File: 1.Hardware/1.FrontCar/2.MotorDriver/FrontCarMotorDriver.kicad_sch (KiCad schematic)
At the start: 10 parts

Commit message: drv
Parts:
- removed IC?: DRV8701ERGER, Package_DFN_QFN:QFN-24-1EP_4x4mm_P0.5mm_EP2.65x2.65mm_ThermalVias, symbol ErBW_s:DRV8701ERGER
- added C? (x3): 1uF, symbol Device:C_Small
- added C?: 10uF, symbol Device:C_Polarized_Small_US
- added C? (x5): (no value), symbol Device:C_Small
- added C? (x2): 0.1uF, symbol Device:C_Small
- added C?: (no value), symbol Device:C_Polarized_Small_US
- added D? (x2): 1N5819WS, Diode_SMD:D_SOD-323, symbol Diode:1N5819WS
- added IC?: DRV8701ERGER, Package_DFN_QFN:QFN-24-1EP_4x4mm_P0.5mm_EP2.65x2.65mm_ThermalVias, symbol ErBW_s:DRV8701ERGER
- added M? (x2): Motor_DC, symbol Motor:Motor_DC
- added Q? (x4): NMOS, ErBW_s:TPH1R403NL, symbol Device:Q_NMOS_GDS
- added Q? (x3): (no value), ErBW_s:TPH1R403NL, symbol Device:Q_NMOS_GDS
- added Q?: (no value), symbol Device:Q_NMOS_GDS
- added R?: (no value), symbol Device:R_Small
- added R?: 50mR, symbol Device:R_Small
- IC?: value (none) -> SN74LVC244APW; footprint (none) -> SOP65P640X120-20N
- IC?: value (none) -> DRV8701ERGER; footprint (none) -> Package_DFN_QFN:QFN-24-1EP_4x4mm_P0.5mm_EP2.65x2.65mm_ThermalVias
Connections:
- net GNDPWR: now also IC?.16 (GND_2), IC?.20 (SN), IC?.25 (GND_3), IC?.5 (GND_1), C?.1, C?.1, C?.2, C?.2, C?.2, C?.2, C?.2, C?.2, IC?.16 (GND_2), IC?.20 (SN), IC?.25 (GND_3), IC?.5 (GND_1), R?.2, R?.2
- net at IC?.1 (VM): now also C?.1, C?.1, C?.2, D?.1 (K)
- net at IC?.12 (IDRIVE): now also IC?.6 (VREF), IC?.7 (AVDD), C?.1
- net at IC?.17 (GH1): now also Q?.1 (G)
- net at IC?.18 (SH1): now also M?.2 (-), Q?.2 (D), Q?.3 (S)
- net at IC?.19 (GL1): now also Q?.1 (G)
- net at IC?.2 (VCP): now also C?.2
- net at IC?.21 (SP): now also Q?.2 (D), Q?.3 (S), R?.1
- net at IC?.22 (GL2): now also Q?.1 (G)
- net at IC?.23 (SH2): now also M?.1 (+), Q?.2 (D), Q?.3 (S)
- net at IC?.24 (GH2): now also Q?.1 (G)
- net at IC?.3 (CPH): now also C?.1
- net at IC?.4 (CPL): now also C?.2
- net at IC?.8 (DVDD): now also C?.1
- new net: C?.1, C?.1, C?.2, D?.1 (K), IC?.1 (VM)
- new net: C?.2, IC?.2 (VCP)
- new net: IC?.23 (SH2), M?.1 (+), Q?.2 (D), Q?.3 (S)
- new net: IC?.18 (SH1), M?.2 (-), Q?.2 (D), Q?.3 (S)
- new net: IC?.19 (GL1), Q?.1 (G)
- new net: IC?.21 (SP), Q?.2 (D), Q?.3 (S), R?.1
- new net: C?.1, IC?.8 (DVDD)
- new net: C?.1, IC?.12 (IDRIVE), IC?.6 (VREF), IC?.7 (AVDD)
- new net: IC?.17 (GH1), Q?.1 (G)
- new net: IC?.22 (GL2), Q?.1 (G)
- new net: IC?.24 (GH2), Q?.1 (G)
- new net: C?.1, IC?.3 (CPH)
- new net: C?.2, IC?.4 (CPL)
- no-connect marks 0 -> 6
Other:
- moved on the sheet: C?, D?, IC?, R?, U?

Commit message: 电池接口
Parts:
- added C?: (no value), symbol Device:C_Polarized_Small_US
- added J?: (no value), symbol Connector_Generic:Conn_01x02
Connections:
- net +5V is gone; now on net +7.5V: C?.1, C?.1, U?.3 (VI)
- net GNDPWR: now also C?.2, J?.2 (Pin_2)
- net +7.5V: now reaches Q?.3 (S)
- net +7.5V: now also D?.2 (A), D?.2 (A), Q?.2 (D), Q?.2 (D), Q?.3 (S), C?.1, J?.1 (Pin_1)
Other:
- moved on the sheet: C?, D?, IC?, R?, U?

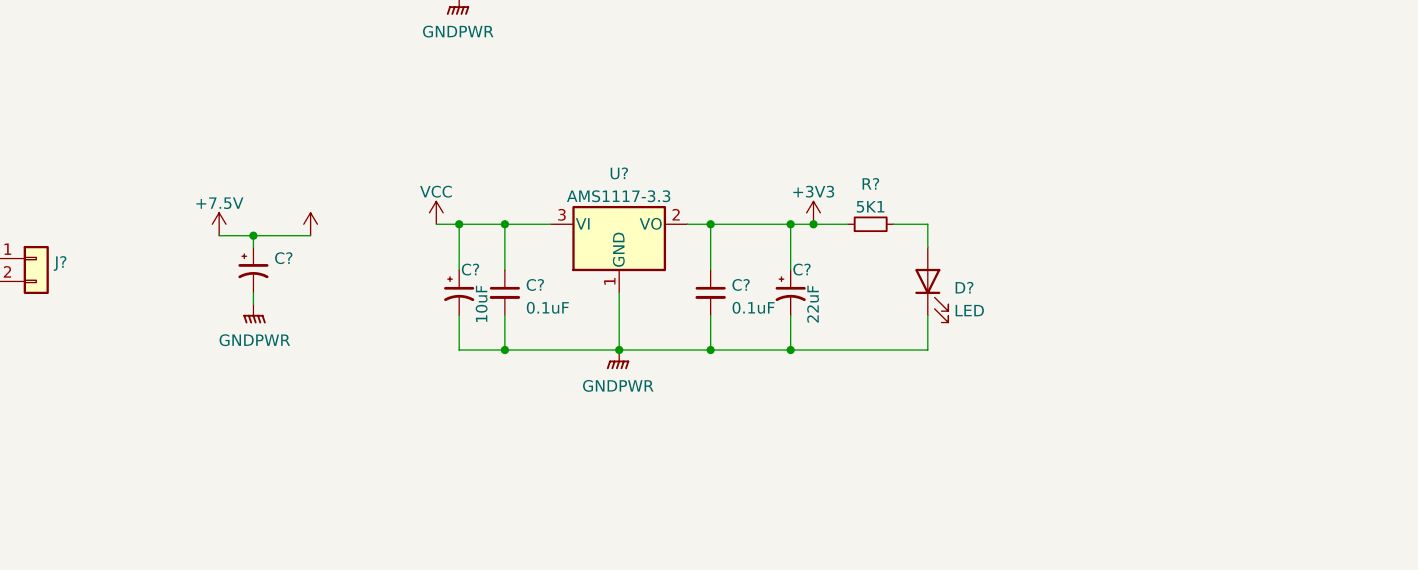
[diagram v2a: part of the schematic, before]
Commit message: 增加一个电源接口
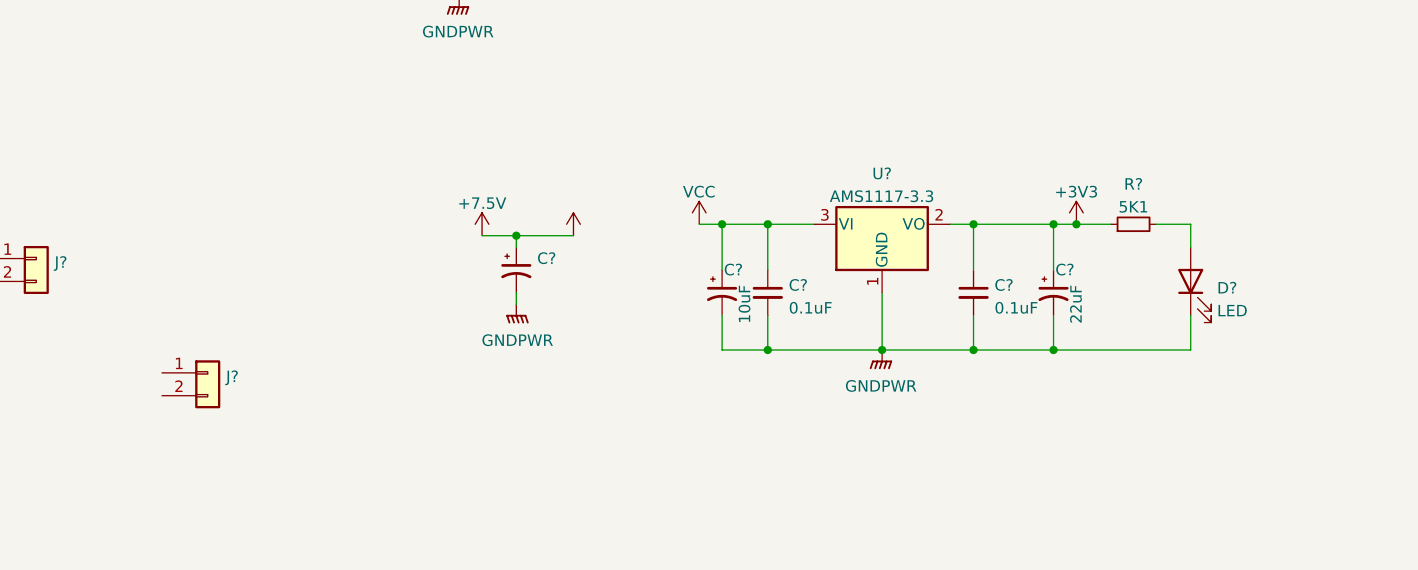
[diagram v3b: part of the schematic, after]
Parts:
- added J?: (no value), symbol Connector_Generic:Conn_01x02
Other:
- moved on the sheet: C?, D?, R?, U?

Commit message: 驱动板电源
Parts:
- added D?: (no value), symbol Diode:1N4148W
- added D?: LED, symbol Device:LED
- added R?: (no value), symbol Device:R_Small
- added SW?: SW_SPDT, symbol Switch:SW_SPDT
- added SW?: (no value), symbol Switch:SW_SPDT
- C?: value (none) -> 470uF
- C? (x3): value (none) -> 1uF
- C? (x2): value (none) -> 0.1uF
- C?: value (none) -> 10uF
- J?: value (none) -> Conn_01x02; footprint (none) -> Connector_AMASS:AMASS_XT30U-F_1x02_P5.0mm_Vertical
- J?: value (none) -> Conn_01x02; footprint (none) -> ErBW_s:BatteryHolder_2x18650
- Q? (x3): value (none) -> NMOS
- Q?: value (none) -> NMOS; footprint (none) -> ErBW_s:TPH1R403NL
- R?: value (none) -> 50mR
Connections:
- net +3V3: now also SW?.2 (B)
- net +7.5V: now also J?.1 (Pin_1), SW?.2 (B); no longer C?.1, C?.1, C?.1, D?.2 (A), D?.2 (A), Q?.2 (D), Q?.2 (D), Q?.3 (S), Q?.3 (S), U?.3 (VI)
- net GNDPWR: now also J?.2 (Pin_2), D?.1 (K)
- net WKUP: now reaches IC?.13 (NSLEEP)
- net WKUP: now also IC?.13 (NSLEEP), R?.1, SW?.1 (A)
- new net: C?.1, D?.2 (A), SW?.1 (A)
- new net: D?.2 (A), R?.2
- new net VCC: C?.1, C?.1, D?.1 (K), D?.2 (A), D?.2 (A), Q?.2 (D), Q?.2 (D), Q?.3 (S), Q?.3 (S), U?.3 (VI)
- no-connect marks 6 -> 8
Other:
- moved on the sheet: C?, D?, J?, R?, U?

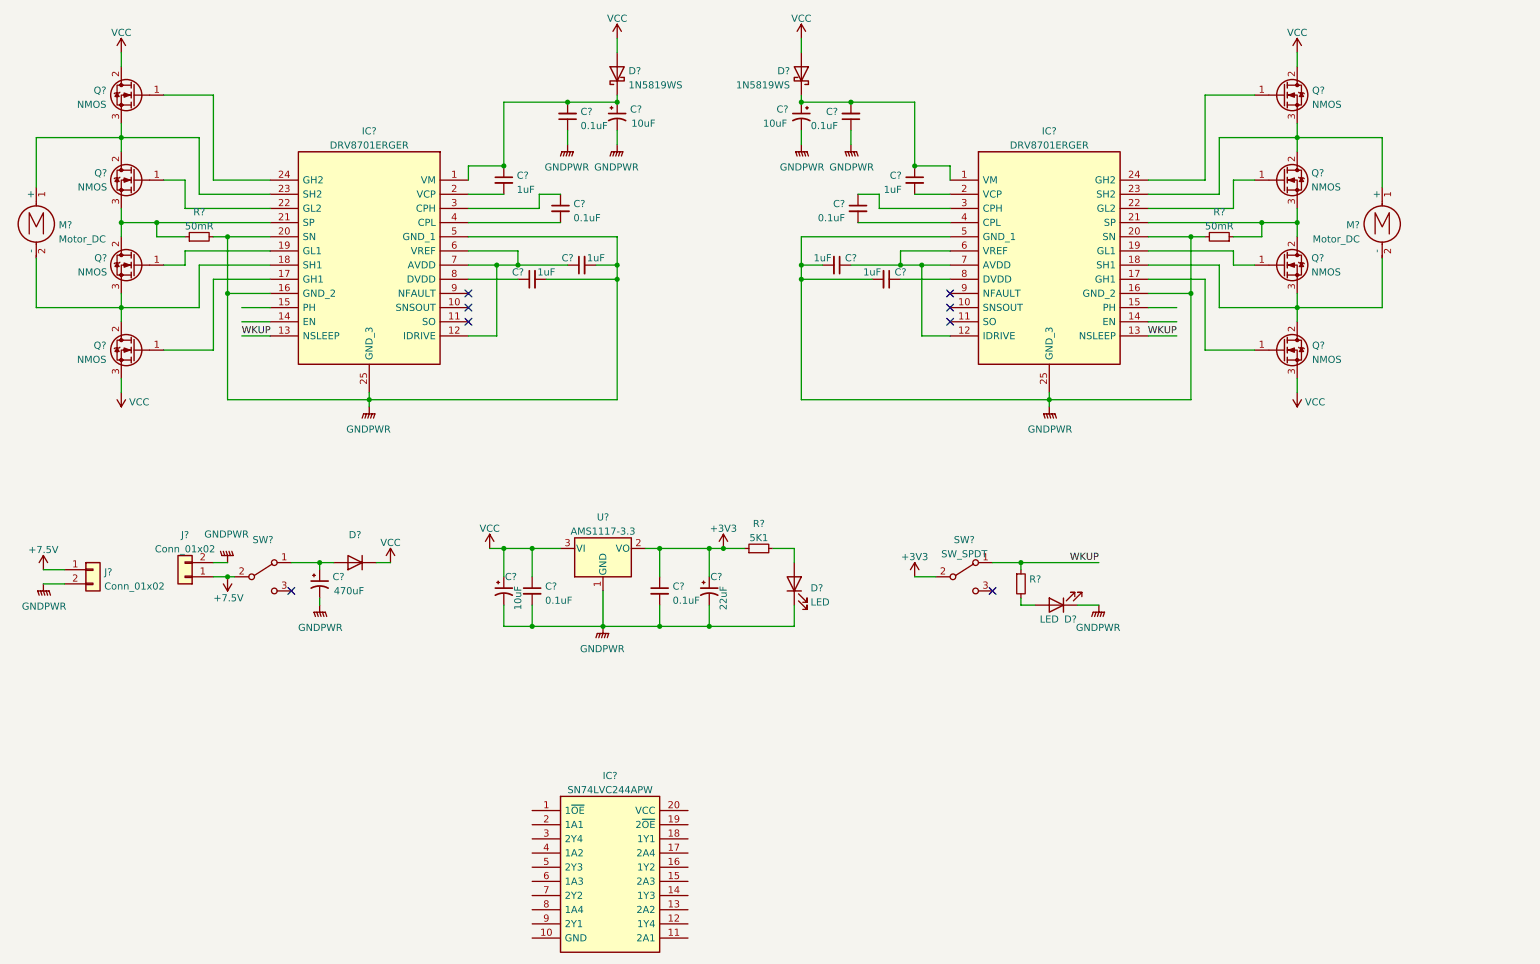
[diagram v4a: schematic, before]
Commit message: 驱动原理图完成
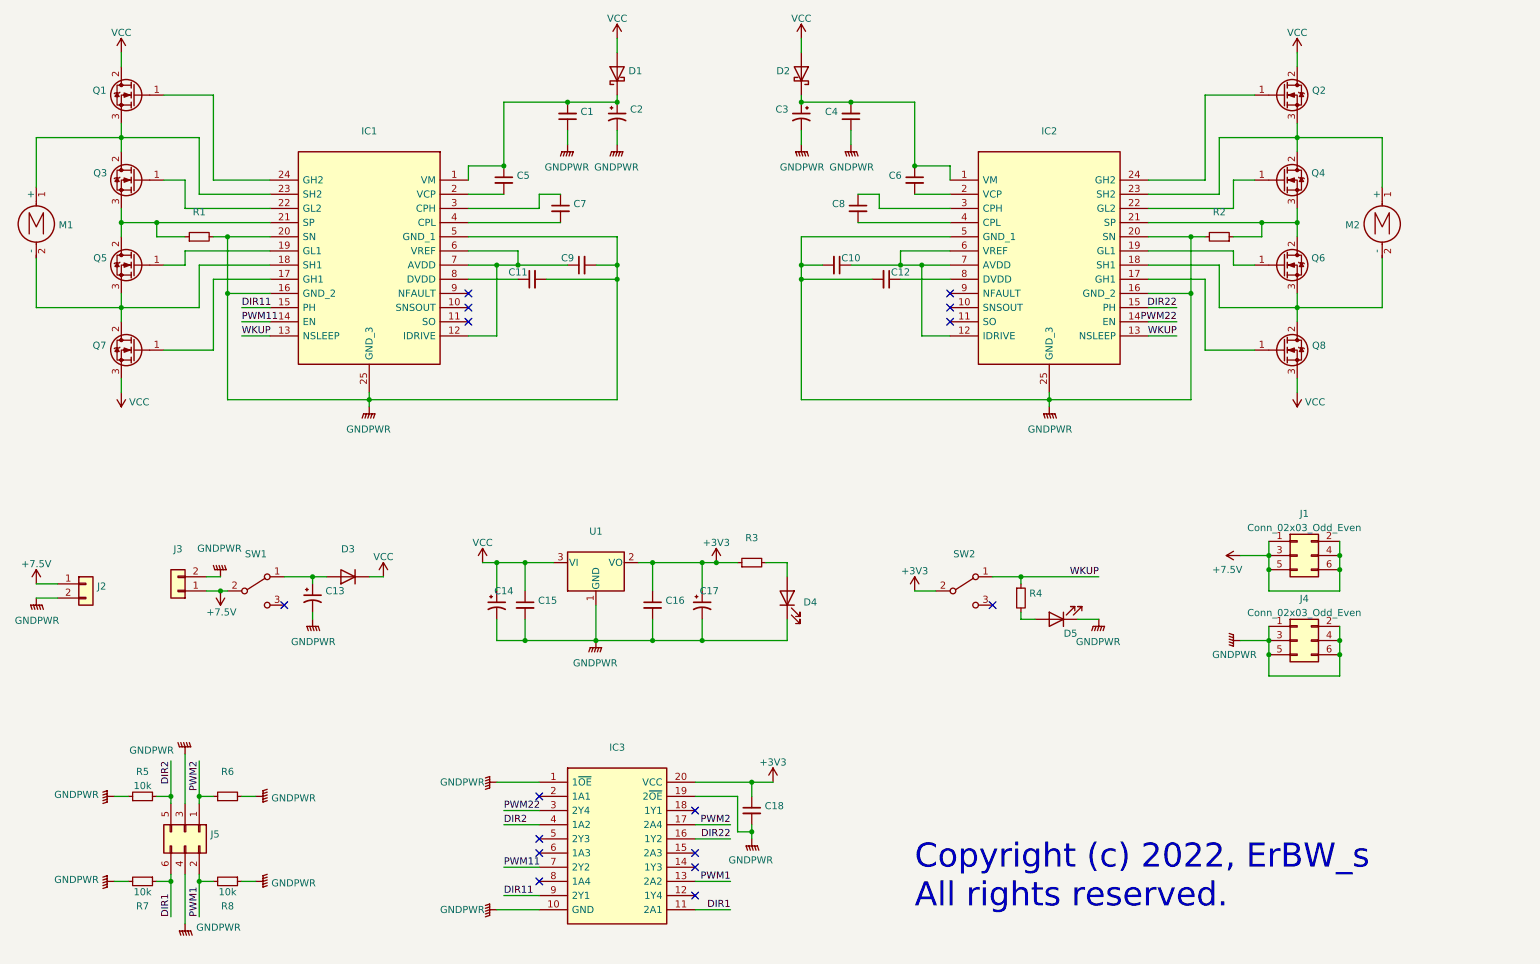
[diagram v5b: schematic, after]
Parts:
- added C18: 0.1uF, symbol Device:C_Small
- added J1, J4: Conn_02x03_Odd_Even, symbol Connector_Generic:Conn_02x03_Odd_Even
- added J5: (no value), symbol Connector_Generic:Conn_02x03_Odd_Even
- added R5, R7, R8: 10k, symbol Device:R_Small
- added R6: (no value), symbol Device:R_Small
- C1, C4, C7, C8: renamed from C?; value 0.1uF -> (none)
- C10, C11, C12, C5, C6, C9: renamed from C?; value 1uF -> (none)
- C13: renamed from C?; value 470uF -> (none)
- C14, C2, C3: renamed from C?; value 10uF -> (none)
- C17: renamed from C?; value 22uF -> (none)
- D1, D2: renamed from D?; value 1N5819WS -> (none); footprint Diode_SMD:D_SOD-323 -> (none)
- D3: renamed from D?; value (none) -> 1N4148W; footprint (none) -> Diode_SMD:D_SOD-123
- IC1, IC2: renamed from IC?; value DRV8701ERGER -> (none); footprint Package_DFN_QFN:QFN-24-1EP_4x4mm_P0.5mm_EP2.65x2.65mm_ThermalVias -> (none)
- IC3: renamed from IC?; value SN74LVC244APW -> (none); footprint SOP65P640X120-20N -> (none)
- J2: renamed from J?; value Conn_01x02 -> (none); footprint Connector_AMASS:AMASS_XT30U-F_1x02_P5.0mm_Vertical -> (none)
- J3: renamed from J?; value Conn_01x02 -> (none); footprint ErBW_s:BatteryHolder_2x18650 -> (none)
- M1, M2: renamed from M?; value Motor_DC -> (none)
- Q1, Q2, Q3, Q4, Q5, Q6, Q7, Q8: renamed from Q?; value NMOS -> (none); footprint ErBW_s:TPH1R403NL -> (none)
- R1, R2: renamed from R?; value 50mR -> (none)
- R4: renamed from R?; value (none) -> 1k
- SW1: renamed from SW?; value (none) -> SW_SPDT
- SW2: renamed from SW?; value SW_SPDT -> (none)
- gave numbers to parts that had none: 6
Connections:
- net +3V3: now also IC3.20 (VCC), C18.1
- net +7.5V: now also J1.1 (Pin_1), J1.2 (Pin_2), J1.3 (Pin_3), J1.4 (Pin_4), J1.5 (Pin_5), J1.6 (Pin_6)
- net GNDPWR: now also IC3.1 (1~{OE}), IC3.10 (GND), IC3.19 (2~{OE}), C18.2, J4.1 (Pin_1), J4.2 (Pin_2), J4.3 (Pin_3), J4.4 (Pin_4), J4.5 (Pin_5), J4.6 (Pin_6), J5.3 (Pin_3), J5.4 (Pin_4), R5.1, R6.2, R7.2, R8.1
- net PWM22: now reaches IC2.14 (EN)
- net PWM22: now also IC3.3 (2Y4)
- net DIR22: now reaches IC2.15 (PH)
- net DIR22: now also IC3.16 (1Y2)
- net DIR1: now reaches IC3.11 (2A1)
- net DIR1: now also J5.6 (Pin_6), R7.1
- net PWM1: now reaches IC3.13 (2A2)
- net PWM1: now also J5.2 (Pin_2), R8.2
- net PWM2: now reaches IC3.17 (2A4)
- net PWM2: now also J5.1 (Pin_1), R6.1
- net DIR2: now reaches IC3.4 (1A2)
- net DIR2: now also J5.5 (Pin_5), R5.2
- net PWM11: now reaches IC3.7 (2Y2)
- net PWM11: now also IC1.14 (EN)
- net DIR11: now reaches IC3.9 (2Y1)
- net DIR11: now also IC1.15 (PH)
- no-connect marks 8 -> 16
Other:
- note added: "Copyright (c) 2022, ErBW_s All rights reserved."
- moved on the sheet: C13, C14, C15, C16, C17, D3, D4, D5, IC3, J2, J3, R3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

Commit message: 驱动pcb初步布局
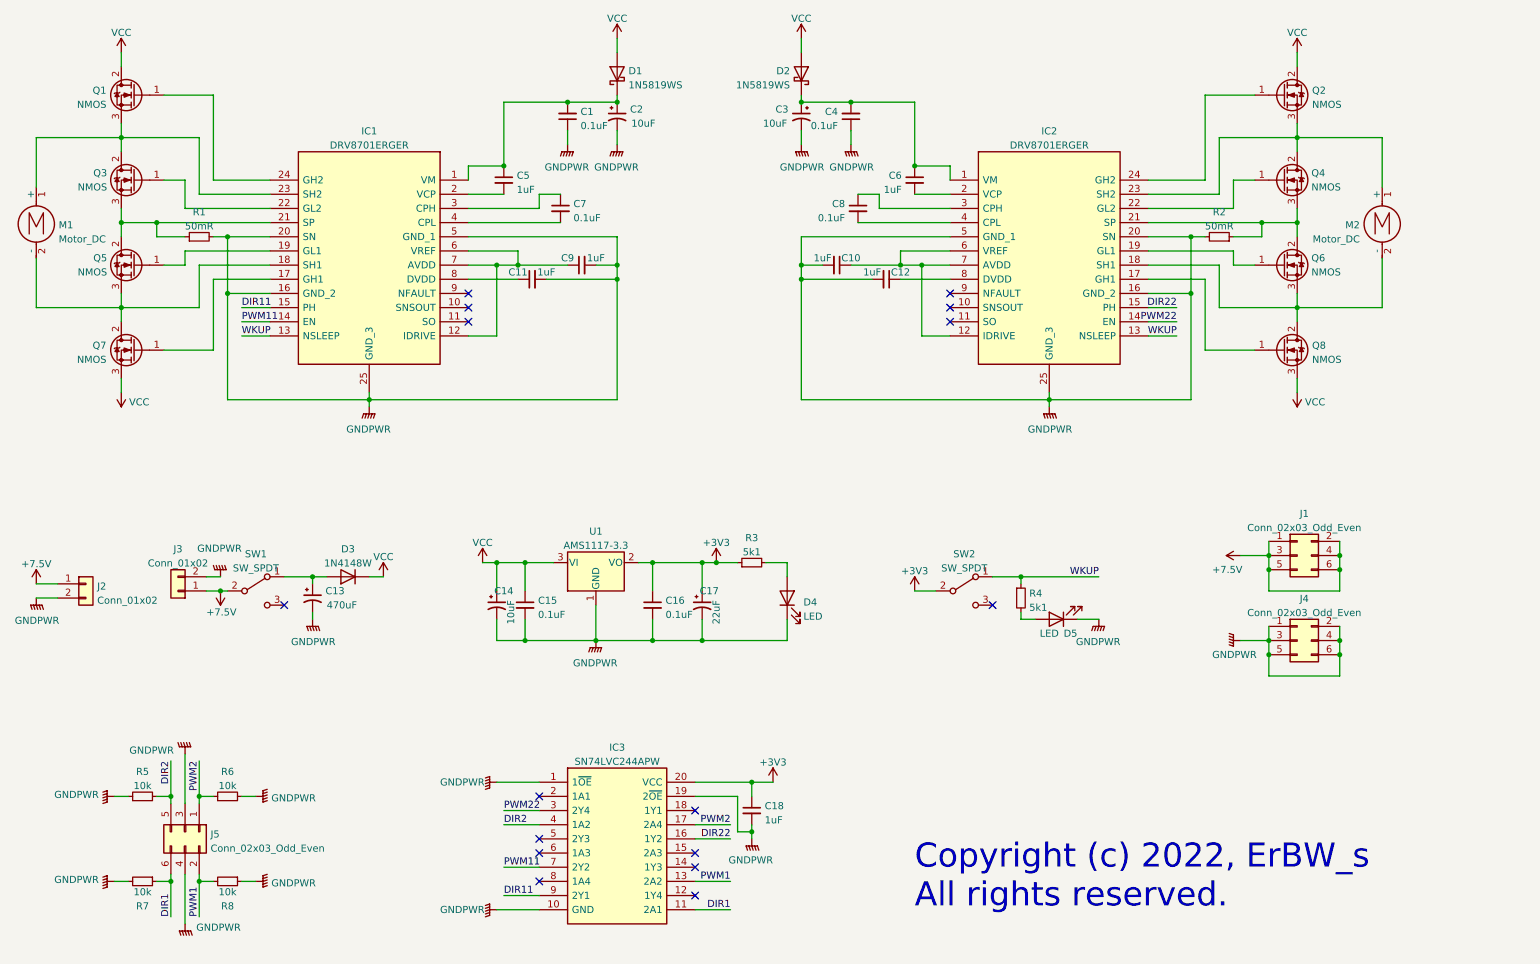
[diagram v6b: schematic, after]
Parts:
- C1, C4, C7, C8: value (none) -> 0.1uF; footprint (none) -> Capacitor_SMD:C_0603_1608Metric
- C10, C11, C12, C5, C6, C9: value (none) -> 1uF; footprint (none) -> Capacitor_SMD:C_0603_1608Metric
- C13: value (none) -> 470uF; footprint (none) -> Capacitor_Tantalum_SMD:CP_EIA-7343-30_AVX-N
- C14, C2, C3: value (none) -> 10uF; footprint (none) -> Capacitor_Tantalum_SMD:CP_EIA-3528-15_AVX-H
- C15, C16, C18: footprint (none) -> Capacitor_SMD:C_0603_1608Metric
- C17: value (none) -> 22uF; footprint (none) -> Capacitor_Tantalum_SMD:CP_EIA-3528-15_AVX-H
- D1, D2: value (none) -> 1N5819WS; footprint (none) -> Diode_SMD:D_SOD-323
- D4, D5: footprint (none) -> LED_SMD:LED_0805_2012Metric
- IC1, IC2: value (none) -> DRV8701ERGER; footprint (none) -> Package_DFN_QFN:QFN-24-1EP_4x4mm_P0.5mm_EP2.65x2.65mm_ThermalVias
- IC3: value (none) -> SN74LVC244APW; footprint (none) -> ErBW_s:SOP65P640X120-20N
- J1, J4: footprint (none) -> Connector_PinSocket_2.54mm:PinSocket_2x03_P2.54mm_Vertical
- J2: value (none) -> Conn_01x02; footprint (none) -> Connector_AMASS:AMASS_XT30U-M_1x02_P5.0mm_Vertical
- J3: value (none) -> Conn_01x02; footprint (none) -> ErBW_s:BatteryHolder_2x18650
- J5: value (none) -> Conn_02x03_Odd_Even; footprint (none) -> Connector_PinSocket_2.54mm:PinSocket_2x03_P2.54mm_Vertical
- M1, M2: value (none) -> Motor_DC; footprint (none) -> Connector_AMASS:AMASS_XT30U-M_1x02_P5.0mm_Vertical
- Q1, Q2, Q3, Q4, Q5, Q6, Q7, Q8: value (none) -> NMOS; footprint (none) -> ErBW_s:DirectFET_ME
- R1, R2: value (none) -> 50mR; footprint (none) -> Resistor_SMD:R_2512_6332Metric
- R3, R5, R7, R8: footprint (none) -> Resistor_SMD:R_0603_1608Metric
- R4: value 1k -> 5k1; footprint (none) -> Resistor_SMD:R_0603_1608Metric
- R6: value (none) -> 10k; footprint (none) -> Resistor_SMD:R_0603_1608Metric
- SW1: footprint (none) -> ErBW_s:SPDT_MTS_102
- SW2: value (none) -> SW_SPDT; footprint (none) -> ErBW_s:SPDT_MTS_102
